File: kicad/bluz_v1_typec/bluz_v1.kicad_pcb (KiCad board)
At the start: 2 copper layers, 24.9 x 14.9 mm, 73 parts, among them J10 Conn, J11 Conn, J12 BTAnt, J2 Conn, J3 Conn, J4 Conn, J5 Conn, J6 Conn, J7 Conn, J8 Conn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

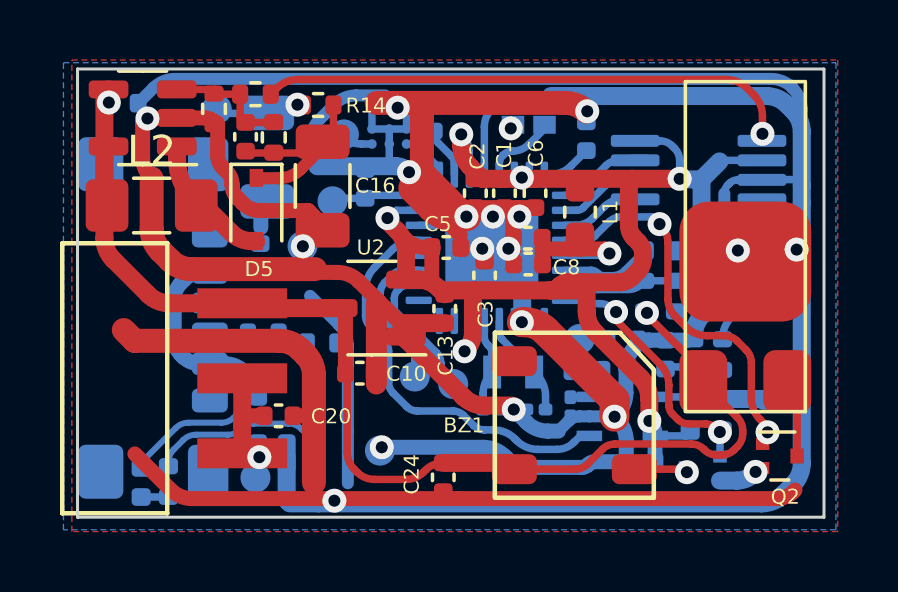
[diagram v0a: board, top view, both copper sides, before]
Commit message: удалено:       kicad/bluz_v1_typec/bluz_v1-backups/bluz_v1-2024-12-26_190152.zip 	удалено:       kicad/bluz_v1_typec/bluz_v1-backups/bluz_v1-2024-12-27_152005.zip 	удалено:       kicad/bluz_v1_typec/bluz_v1-backups/bluz_v1-2025-01-20_122513.zip 	удалено:       kicad/bluz_v1_typec/bluz_v1-backups/bluz_v1-2025-01-21_100500.zip 	удалено:       kicad/bluz_v1_typec/bluz_v1-backups/bluz_v1-2025-01-21_105512.zip 	удалено:       kicad/bluz_v1_typec/bluz_v1-backups/bluz_v1-2025-01-21_110513.zip 	изменено:      kicad/bluz_v1_typec/bluz_v1.kicad_pcb 	изменено:      kicad/bluz_v1_typec/bluz_v1.kicad_pro 	изменено:      kicad/bluz_v1_typec/bluz_v1.kicad_sch 	изменено:      kicad/bluz_v1_typec/fp-info-cache
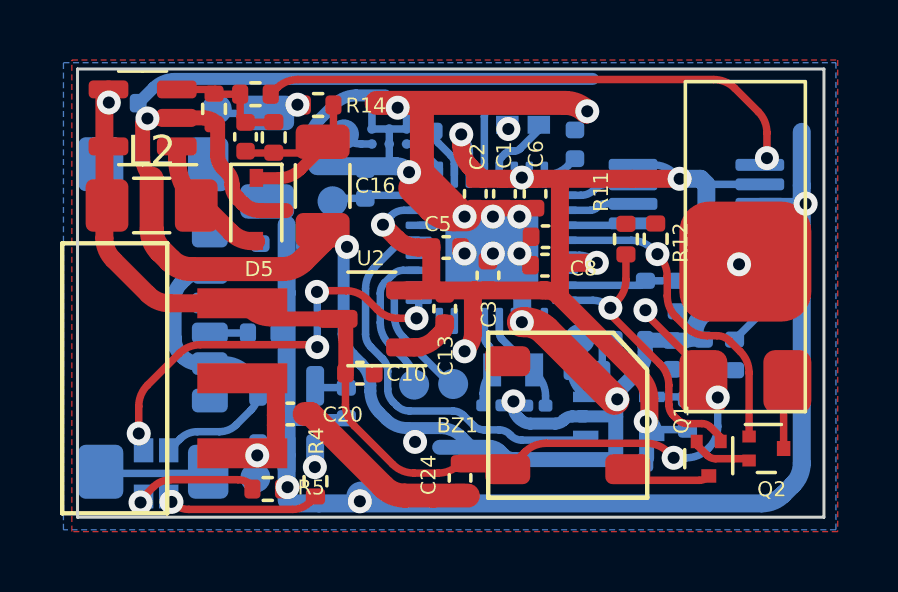
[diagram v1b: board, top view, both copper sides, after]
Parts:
- removed D2: Red, LED_SMD:LED_0402_1005Metric
- removed D3: Green, LED_SMD:LED_0402_1005Metric
- removed L1: 10uH, Inductor_SMD:L_0603_1608Metric
- removed R*1: 3.3k, Resistor_SMD:R_0201_0603Metric
- added LED1: LTST-C195KGJRKT, easyeda2kicad:LED-ARRAY-SMD_0603-4P-L1.6-W1.5-BR-RD, B.Cu at (64.3, 50.6)
- Q1, R11, R12, R4, R5: moved to F.Cu
- moved R5 16.8 mm to (68.0, 51.1)
- moved R12 7.00 mm to (81.0, 42.8)
- moved R11 6.66 mm to (80.0, 42.8)
- moved R4 4.90 mm to (69.6, 50.9), turned to -90 degrees
- moved R3 2.16 mm to (70.7, 48.2), turned to -90 degrees
- moved J7 1.65 mm to (71.2, 51.4)
- moved C11 0.87 mm to (83.1, 43.6)
- moved D4 0.80 mm to (82.3, 41.3)
- moved C23 0.59 mm to (77.3, 42.7)
- moved C8 0.56 mm to (77.3, 43.6)
- moved C24 0.56 mm to (74.5, 50.7)
- moved Q2 0.51 mm to (84.7, 49.8)
- moved C7 0.47 mm to (78.3, 39.6)
- moved R8 0.40 mm to (83.6, 46.6)
- moved C20 0.39 mm to (68.8, 48.6)
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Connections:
- net Net-(D2-A) renamed vbus
- C23 pad 1: Net-(D1-VDA) -> +2V8
- C8 pad 1: Net-(D1-VDA) -> +2V8
- D1 pad 17: unconnected-(D1-PA15-Pad17) -> LED
- D1 pad 5: Net-(D1-VDA) -> +2V8
- D1 pad 6: LED -> unconnected-(D1-PA5-Pad6)
- R4 pad 1: Net-(D2-K) -> stat
- R4 pad 2: Net-(U1-STAT) -> Net-(LED1---Pad4)
- U1 pad 1: Net-(U1-STAT) -> stat
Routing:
- net GND: track 208.7 -> 154.2 mm, vias 19 -> 20
- net LED: track 3.03 -> 13.9 mm, vias 0 -> 4
- net Net-(U1-STAT): track 6.71 -> 0.00 mm
- net Net-(D1-VDA): track 5.44 -> 0.00 mm, vias 1 -> 0
- net Net-(LED1---Pad4): track 0.00 -> 5.00 mm, vias 0 -> 1
- net +2V8: track 48.2 -> 44.2 mm, vias 6 -> 7
- net Net-(LED1---Pad3): track 1.13 -> 4.13 mm, vias 0 -> 1
- net Vibro: track 12.9 -> 10.9 mm, vias 2 -> 1
- net Sound: track 8.54 -> 9.89 mm, vias 2 -> 1
- net vbus: track 13.2 -> 12.1 mm
- net cmpAdj: track 5.31 -> 4.29 mm
- net A_SDI: track 3.31 -> 2.36 mm
- net +BATT: track 38.4 -> 37.4 mm, vias 2 -> 4
- net Net-(D2-K): track 0.91 -> 0.00 mm
- net /B+: track 3.23 -> 2.50 mm
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
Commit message: удалено:       kicad/bluz_v1_typec/bluz_v1-backups/bluz_v1-2025-01-22_110710.zip 	удалено:       kicad/bluz_v1_typec/bluz_v1-backups/bluz_v1-2025-01-28_102500.zip 	удалено:       kicad/bluz_v1_typec/bluz_v1-backups/bluz_v1-2025-01-28_134021.zip 	удалено:       kicad/bluz_v1_typec/bluz_v1-backups/bluz_v1-2025-02-11_170038.zip 	удалено:       kicad/bluz_v1_typec/bluz_v1-backups/bluz_v1-2025-02-25_125512.zip 	изменено:      kicad/bluz_v1_typec/bluz_v1.kicad_pcb 	изменено:      kicad/bluz_v1_typec/bluz_v1.kicad_prl 	изменено:      kicad/bluz_v1_typec/bluz_v1.kicad_pro 	изменено:      kicad/bluz_v1_typec/bluz_v1.kicad_sch 	изменено:      kicad/bluz_v1_typec/fp-info-cache 	изменено:      kicad/bluz_v1_typec/gerber/BluZ.zip 	удалено:       kicad/bluz_v1_typec/gerber/bluz_v1-job.gbrjob 	изменено:      kicad/bluz_v1_typec/gerber/mk-gerber.sh 	изменено:      kicad/bluz_v1_typec/gerber/mk-gerber.sh~
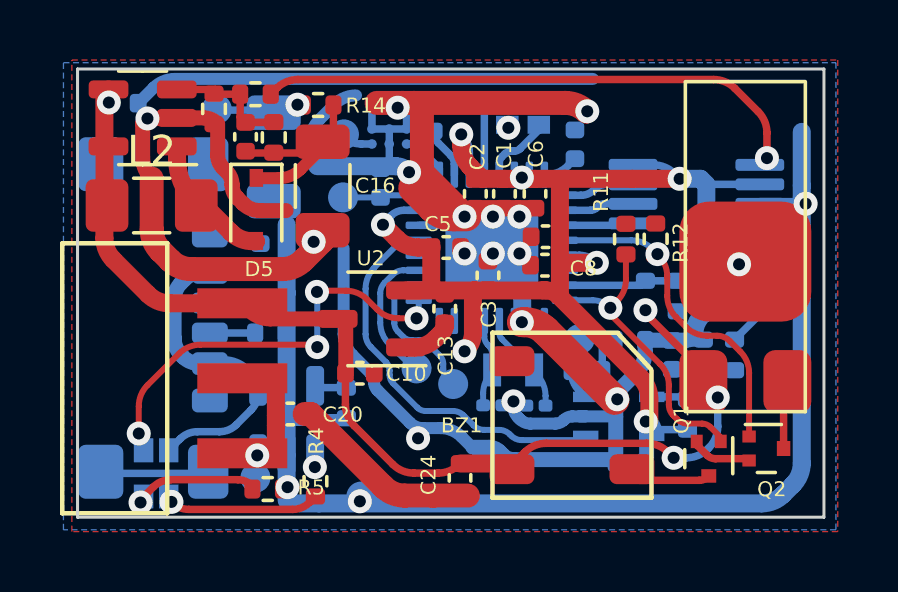
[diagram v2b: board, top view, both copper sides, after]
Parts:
- BZ1: footprint My-library:Buzzer55x55 -> lib:Buzzer55x55
- R5: value 1k -> 33
- moved J4 0.55 mm to (73.0, 47.1)
- moved C18 0.51 mm to (71.8, 40.9)
- moved J2 0.37 mm to (70.5, 41.4)
- moved R17 0.24 mm to (68.1, 45.9)
- moved R18 0.24 mm to (68.1, 44.9)
- moved C19 0.22 mm to (68.2, 40.0)
- moved J10 0.17 mm to (69.6, 42.9)
- moved BZ1 0.14 mm to (78.2, 48.6)
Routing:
- net GND: track 154.2 -> 151.2 mm

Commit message: удалено:       kicad/bluz_v1_typec/bluz_v1-backups/bluz_v1-2025-03-25_124207.zip 	удалено:       kicad/bluz_v1_typec/bluz_v1-backups/bluz_v1-2025-03-25_145630.zip 	изменено:      kicad/bluz_v1_typec/bluz_v1.kicad_pcb 	изменено:      kicad/bluz_v1_typec/bluz_v1.kicad_prl 	изменено:      kicad/bluz_v1_typec/bluz_v1.kicad_sch
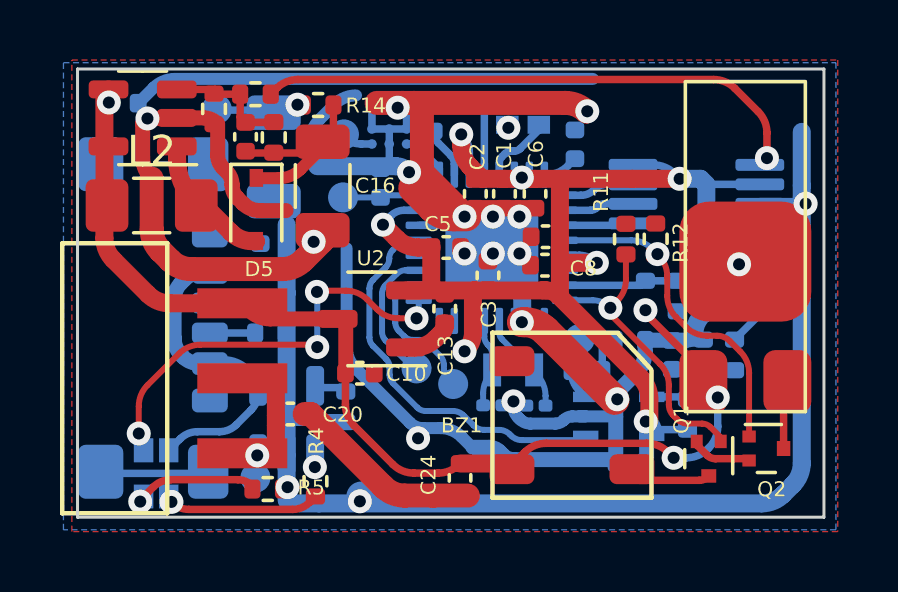
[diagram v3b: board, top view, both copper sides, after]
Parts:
- moved R3 0.13 mm to (70.6, 48.4)

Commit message: изменено:      kicad/bluz_v1_typec/bluz_v1.kicad_pcb 	изменено:      kicad/bluz_v1_typec/bluz_v1.kicad_prl 	изменено:      kicad/bluz_v1_typec/bluz_v1.kicad_sch 	изменено:      stm32cubeide/BluZ_LPM/.mxproject 	изменено:      stm32cubeide/BluZ_LPM/BluZ_LPM.ioc 	изменено:      stm32cubeide/BluZ_LPM/Core/Inc/main.h 	изменено:      stm32cubeide/BluZ_LPM/Core/Src/main.c 	изменено:      stm32cubeide/BluZ_LPM/Release/BluZ_LPM.elf
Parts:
- D5: value BAT46JFILM -> BAS16
- R17, R18: value 56k -> 5.1k
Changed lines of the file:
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@@
 			)
 		)
-		(property "Datasheet" "~"
+		(property "Datasheet" ""
 			(at 0 0 270)
 			(layer "F.Fab")
@@
 			)
 		)
-		(property "Datasheet" "~"
+		(property "Datasheet" ""
 			(at 0 0 90)
 			(layer "F.Fab")
@@
 			)
 		)
-		(property "Datasheet" "~"
+		(property "Datasheet" ""
 			(at 0 0 0)
 			(layer "F.Fab")
@@
 			)
 		)
-		(property "Datasheet" "~"
+		(property "Datasheet" ""
 			(at 0 0 180)
 			(layer "F.Fab")
@@
 			)
 		)
-		(property "Datasheet" "~"
+		(property "Datasheet" ""
 			(at 0 0 180)
 			(layer "B.Fab")
@@
 			)
 		)
-		(property "Datasheet" "~"
+		(property "Datasheet" ""
 			(at 0 0 270)
 			(layer "F.Fab")
@@
 			)
 		)
-		(property "Datasheet" "~"
+		(property "Datasheet" ""
 			(at 0 0 270)
 			(layer "F.Fab")
@@
 			)
 		)
-		(property "Datasheet" "~"
+		(property "Datasheet" ""
 			(at 0 0 180)
 			(layer "F.Fab")
@@
 			)
 		)
-		(property "Datasheet" "~"
+		(property "Datasheet" ""
 			(at 0 0 270)
 			(layer "F.Fab")
@@
 			)
 		)
-		(property "Datasheet" "~"
+		(property "Datasheet" ""
 			(at 0 0 180)
 			(layer "F.Fab")
@@
 			)
 		)
-		(property "Datasheet" "~"
+		(property "Datasheet" ""
 			(at 0 0 270)
 			(layer "F.Fab")
@@
 			)
 		)
-		(property "Datasheet" "~"
+		(property "Datasheet" ""
 			(at 0 0 90)
 			(layer "F.Fab")
@@
 			)
 		)
-		(property "Datasheet" "~"
+		(property "Datasheet" ""
 			(at 0 0 90)
 			(layer "B.Fab")
@@
 			)
 		)
-		(property "Datasheet" "~"
+		(property "Datasheet" ""
 			(at 0 0 0)
 			(layer "F.Fab")
@@
 			)
 		)
-		(property "Datasheet" "~"
+		(property "Datasheet" ""
 			(at 0 0 90)
 			(layer "F.Fab")
@@
 			)
 		)
-		(property "Value" "BAT46JFILM"
+		(property "Value" "BAS16"
 			(at 0.1 1.9 90)
 			(layer "F.Fab")
@@
 			)
 		)
-		(property "Datasheet" "~"
+		(property "Datasheet" ""
 			(at 0 0 270)
 			(layer "F.Fab")
@@
 			)
 		)
-		(property "Datasheet" "~"
+		(property "Datasheet" ""
 			(at 0 0 0)
 			(layer "F.Fab")
@@
 			)
 		)
-		(property "Datasheet" "~"
+		(property "Datasheet" ""
 			(at 0 0 90)
 			(layer "B.Fab")
@@
 			)
 		)
-		(property "Datasheet" "~"
+		(property "Datasheet" ""
 			(at 0 0 90)
 			(layer "F.Fab")
@@
 			)
 		)
-		(property "Datasheet" "~"
+		(property "Datasheet" ""
 			(at 0 0 90)
 			(layer "B.Fab")
@@
 			)
 		)
-		(property "Datasheet" "~"
+		(property "Datasheet" ""
 			(at 0 0 90)
 			(layer "B.Fab")
@@
 			)
 		)
-		(property "Datasheet" "~"
+		(property "Datasheet" ""
 			(at 0 0 0)
 			(layer "F.Fab")
@@
 			)
 		)
-		(property "Datasheet" "~"
+		(property "Datasheet" ""
 			(at 0 0 0)
 			(layer "F.Fab")
@@
 			)
 		)
-		(property "Datasheet" "~"
+		(property "Datasheet" ""
 			(at 0 0 90)
 			(layer "F.Fab")
@@
 			)
 		)
-		(property "Datasheet" "~"
+		(property "Datasheet" ""
 			(at 0 0 180)
 			(layer "F.Fab")
@@
 			)
 		)
-		(property "Datasheet" "~"
+		(property "Datasheet" ""
 			(at 0 0 90)
 			(layer "F.Fab")
@@
 			)
 		)
-		(property "Datasheet" "~"
+		(property "Datasheet" ""
 			(at 0 0 270)
 			(layer "F.Fab")
@@
 			)
 		)
-		(property "Datasheet" "~"
+		(property "Datasheet" ""
 			(at 0 0 0)
 			(layer "F.Fab")
@@
 			)
 		)
-		(property "Datasheet" "~"
+		(property "Datasheet" ""
 			(at 0 0 270)
 			(layer "F.Fab")
@@
 			)
 		)
-		(property "Datasheet" "~"
+		(property "Datasheet" ""
 			(at 0 0 270)
 			(layer "F.Fab")
@@
 			)
 		)
-		(property "Datasheet" "~"
+		(property "Datasheet" ""
 			(at 0 0 270)
 			(layer "F.Fab")
@@
 			)
 		)
-		(property "Datasheet" "~"
+		(property "Datasheet" ""
 			(at 0 0 270)
 			(layer "F.Fab")
@@
 			)
 		)
-		(property "Datasheet" "~"
+		(property "Datasheet" ""
 			(at 0 0 180)
 			(layer "F.Fab")
@@
 			)
 		)
-		(property "Datasheet" "~"
+		(property "Datasheet" ""
 			(at 0 0 180)
 			(layer "F.Fab")
@@
 			)
 		)
-		(property "Datasheet" "~"
+		(property "Datasheet" ""
 			(at 0 0 90)
 			(layer "F.Fab")
@@
 			)
 		)
-		(property "Datasheet" "~"
+		(property "Datasheet" ""
 			(at 0 0 180)
 			(layer "F.Fab")
@@
 			)
 		)
-		(property "Value" "56k"
+		(property "Value" "5.1k"
 			(at 0 -1.17 0)
 			(layer "B.Fab")
@@
 			)
 		)
-		(property "Datasheet" "~"
+		(property "Datasheet" ""
 			(at 0 0 0)
 			(layer "B.Fab")
@@
 			)
 		)
-		(property "Datasheet" "~"
+		(property "Datasheet" ""
 			(at 0 0 180)
 			(layer "F.Fab")
@@
 			)
 		)
-		(property "Datasheet" "~"
+		(property "Datasheet" ""
 			(at 0 0 90)
 			(layer "F.Fab")
@@
 			)
 		)
-		(property "Datasheet" "~"
+		(property "Datasheet" ""
 			(at 0 0 90)
 			(layer "F.Fab")
@@
 			)
 		)
-		(property "Datasheet" "~"
+		(property "Datasheet" ""
 			(at 0 0 180)
 			(layer "F.Fab")
@@
 			)
 		)
-		(property "Datasheet" "~"
+		(property "Datasheet" ""
 			(at 0 0 180)
 			(layer "F.Fab")
@@
 			)
 		)
-		(property "Datasheet" "~"
+		(property "Datasheet" ""
 			(at 0 0 0)
 			(layer "F.Fab")
@@
 			)
 		)
-		(property "Value" "56k"
+		(property "Value" "5.1k"
 			(at 0 -1.17 0)
 			(layer "B.Fab")
@@
 			)
 		)
-		(property "Datasheet" "~"
+		(property "Datasheet" ""
 			(at 0 0 0)
 			(layer "B.Fab")
@@
 			)
 		)
-		(property "Datasheet" "~"
+		(property "Datasheet" ""
 			(at 0 0 180)
 			(layer "F.Fab")
@@
 			)
 		)
-		(property "Datasheet" "~"
+		(property "Datasheet" ""
 			(at 0 0 180)
 			(layer "F.Fab")
@@
 			)
 		)
-		(property "Datasheet" "~"
+		(property "Datasheet" ""
 			(at 0 0 90)
 			(layer "F.Fab")
@@
 			)
 		)
-		(property "Datasheet" "~"
+		(property "Datasheet" ""
 			(at 0 0 180)
 			(layer "F.Fab")
@@
 			)
 		)
-		(property "Datasheet" "~"
+		(property "Datasheet" ""
 			(at 0 0 0)
 			(layer "F.Fab")
@@
 			)
 		)
-		(property "Datasheet" "~"
+		(property "Datasheet" ""
 			(at 0 0 180)
 			(layer "F.Fab")
@@
 			)
 		)
-		(property "Datasheet" "~"
+		(property "Datasheet" ""
 			(at 0 0 90)
 			(layer "F.Fab")
@@
 			)
 		)
-		(property "Datasheet" "~"
+		(property "Datasheet" ""
 			(at 0 0 90)
 			(layer "F.Fab")
@@
 			)
 		)
-		(property "Datasheet" "~"
+		(property "Datasheet" ""
 			(at 0 0 180)
 			(layer "F.Fab")
@@
 			)
 		)
-		(property "Datasheet" "~"
+		(property "Datasheet" ""
 			(at 0 0 0)
 			(layer "F.Fab")

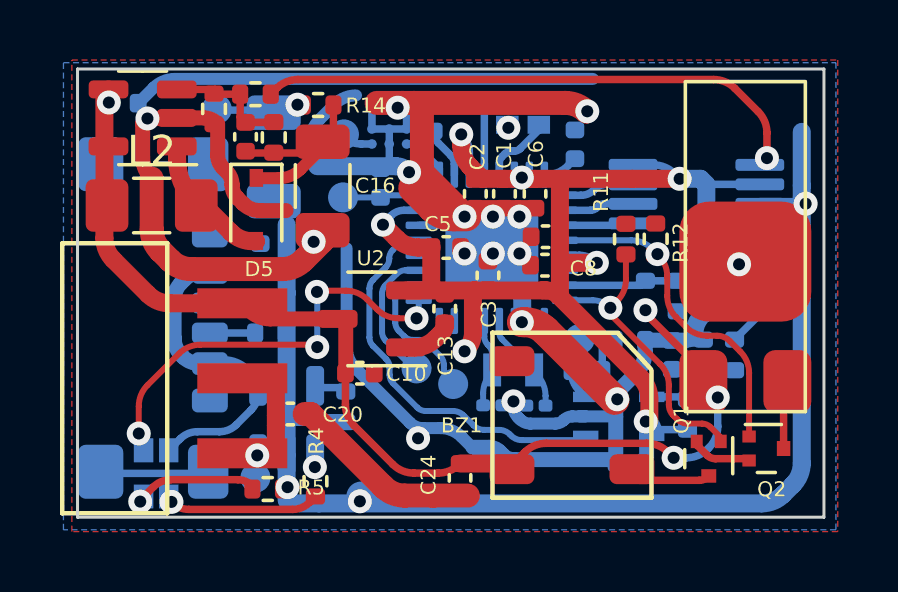
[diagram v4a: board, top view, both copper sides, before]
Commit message: удалено:       kicad/bluz_v1_typec/bluz_v1-backups/bluz_v1-2025-03-25_184904.zip 	удалено:       kicad/bluz_v1_typec/bluz_v1-backups/bluz_v1-2025-05-30_173628.zip 	удалено:       kicad/bluz_v1_typec/bluz_v1-backups/bluz_v1-2025-05-30_190015.zip 	изменено:      kicad/bluz_v1_typec/bluz_v1.kicad_pcb 	изменено:      kicad/bluz_v1_typec/bluz_v1.kicad_prl 	изменено:      kicad/bluz_v1_typec/bom/ibom.html
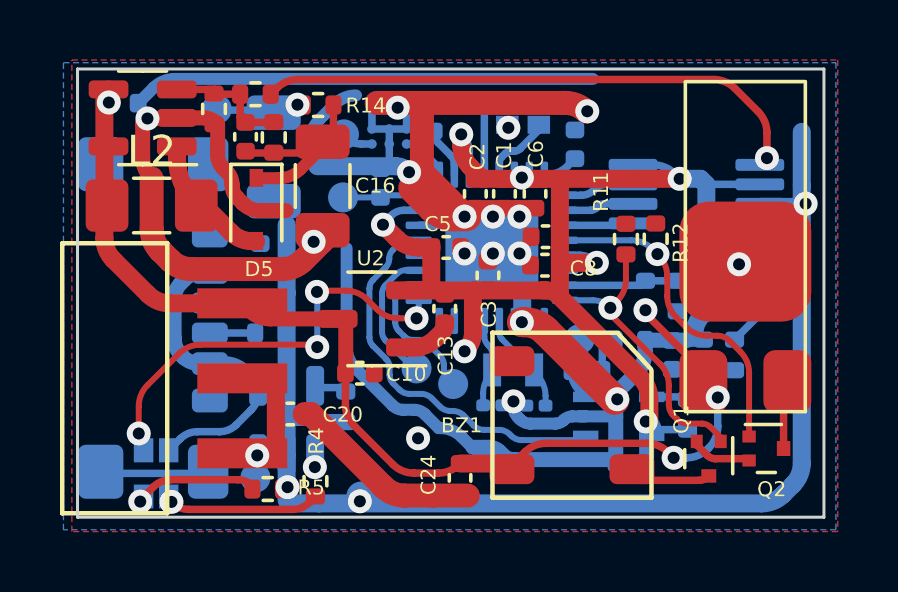
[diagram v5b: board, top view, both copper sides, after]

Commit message: удалено:       kicad/bluz_v1_typec/bluz_v1-backups/bluz_v1-2025-06-09_170559.zip 	удалено:       kicad/bluz_v1_typec/bluz_v1-backups/bluz_v1-2025-06-09_180824.zip 	удалено:       kicad/bluz_v1_typec/bluz_v1-backups/bluz_v1-2025-06-19_095726.zip 	удалено:       kicad/bluz_v1_typec/bluz_v1-backups/bluz_v1-2025-08-04_163535.zip 	изменено:      kicad/bluz_v1_typec/bluz_v1.kicad_pcb 	изменено:      kicad/bluz_v1_typec/bluz_v1.kicad_prl 	изменено:      kicad/bluz_v1_typec/bluz_v1.kicad_sch
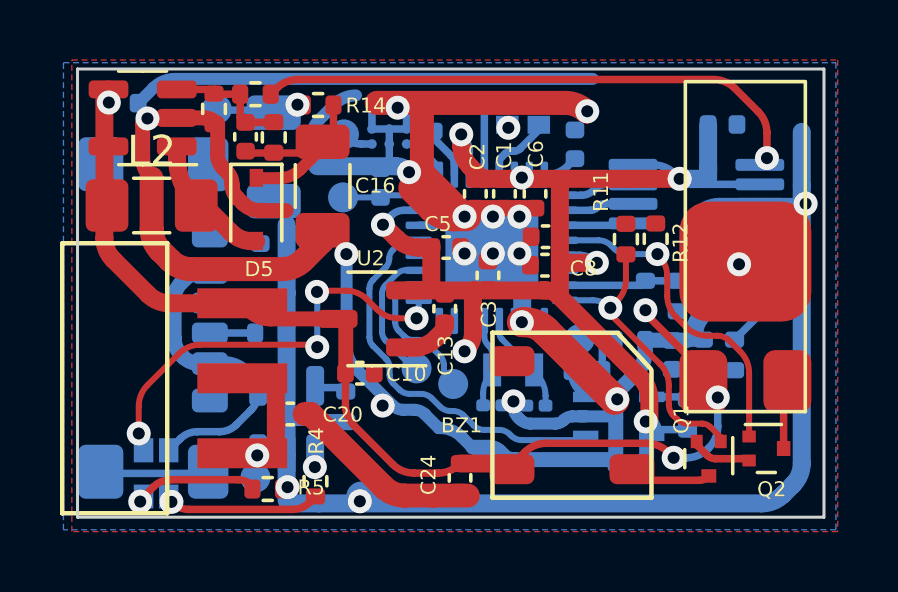
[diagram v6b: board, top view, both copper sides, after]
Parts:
- R5: value 33 -> 82
- moved C11 4.64 mm to (83.2, 39.0)

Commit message: изменено:      Android/BluZ_LPM/BluZ/src/main/java/ru/starline/bluz/MainActivity.kt 	изменено:      kicad/bluz_v1_typec/bluz_v1.kicad_pcb 	изменено:      kicad/bluz_v1_typec/bluz_v1.kicad_sch
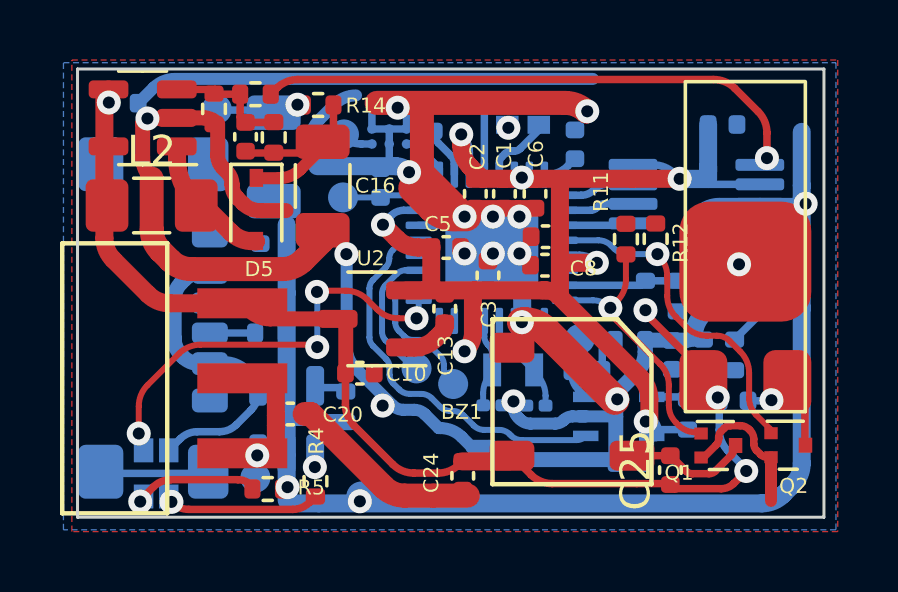
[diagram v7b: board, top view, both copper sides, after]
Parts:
- added C25: 47n, Capacitor_SMD:C_0402_1005Metric, F.Cu at (81.5, 50.5)
- added C26: 47n, Capacitor_SMD:C_0402_1005Metric, B.Cu at (83.6, 48.2)
- moved Q2 0.74 mm to (85.4, 49.6)
- moved Q1 0.54 mm to (83.1, 49.7), turned to 0 degrees
- moved BZ1 0.45 mm to (78.2, 48.2)
- moved C24 0.11 mm to (74.5, 50.7)
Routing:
- net GND: track 151.5 -> 154.6 mm
- net Net-(BZ1-+): track 2.34 -> 4.17 mm
- net +BATT: track 37.4 -> 39.2 mm
- net Net-(Q2-D): track 2.28 -> 3.15 mm, vias 0 -> 1
- net Sound: track 9.89 -> 9.04 mm
